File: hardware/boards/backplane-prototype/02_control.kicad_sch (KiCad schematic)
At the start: 14 parts, among them J10 TC2030-IDC-NL SWD, U1 STM32C092GCU6

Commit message: checkpoint before I2C pin move
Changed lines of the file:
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@@
+	(wire
+		(pts
+			(xy 143.51 100.33) (xy 137.16 100.33)
+		)
+		(stroke
+			(width 0)
+			(type default)
+		)
+	)
 	(wire
 		(pts
@@
 		)
 	)
+	(wire
+		(pts
+			(xy 143.51 102.87) (xy 137.16 102.87)
+		)
+		(stroke
+			(width 0)
+			(type default)
+		)
+	)
+	(wire
+		(pts
+			(xy 87.63 105.41) (xy 101.6 105.41)
+		)
+		(stroke
+			(width 0)
+			(type default)
+		)
+	)
 	(label "NRST"
-		(at 101.6 72.39 0)
+		(at 101.6 72.39 180)
 		(effects
 			(font
 				(size 1.27 1.27)
 			)
-			(justify left bottom)
+			(justify right bottom)
 		)
 	)
@@
 	)
 	(label "LED_DATA_RAW"
-		(at 101.6 105.41 180)
+		(at 87.63 105.41 180)
 		(effects
 			(font
@@
 	)
 	(label "SWCLK"
-		(at 137.16 102.87 180)
+		(at 143.51 102.87 0)
 		(effects
 			(font
 				(size 1.27 1.27)
 			)
-			(justify right bottom)
+			(justify left bottom)
 		)
 	)
@@
 	)
 	(label "SWDIO"
-		(at 137.16 100.33 180)
+		(at 143.51 100.33 0)
 		(effects
 			(font
 				(size 1.27 1.27)
 			)
-			(justify right bottom)
+			(justify left bottom)
 		)
 	)

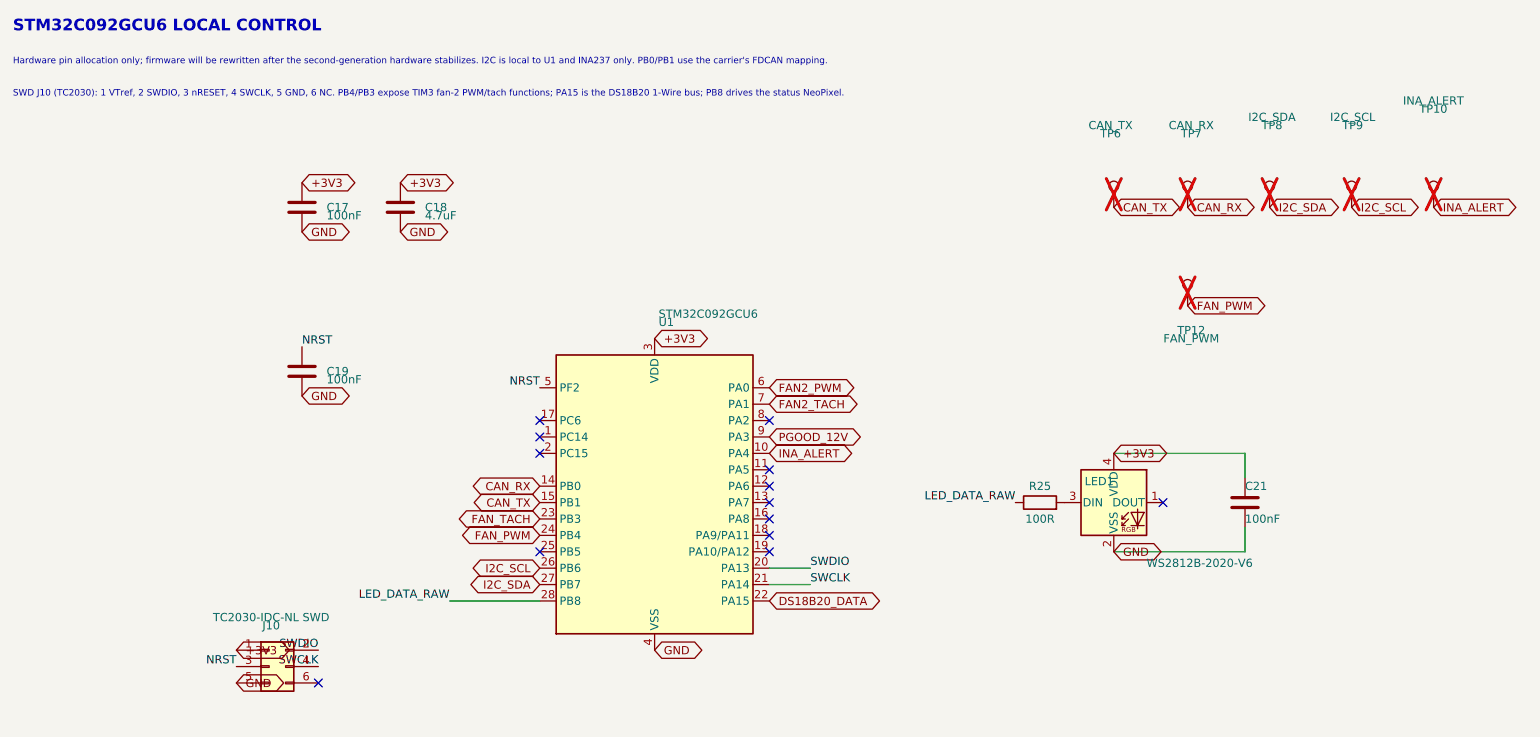
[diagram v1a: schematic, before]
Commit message: move backplane I2C to PA6 and PA7
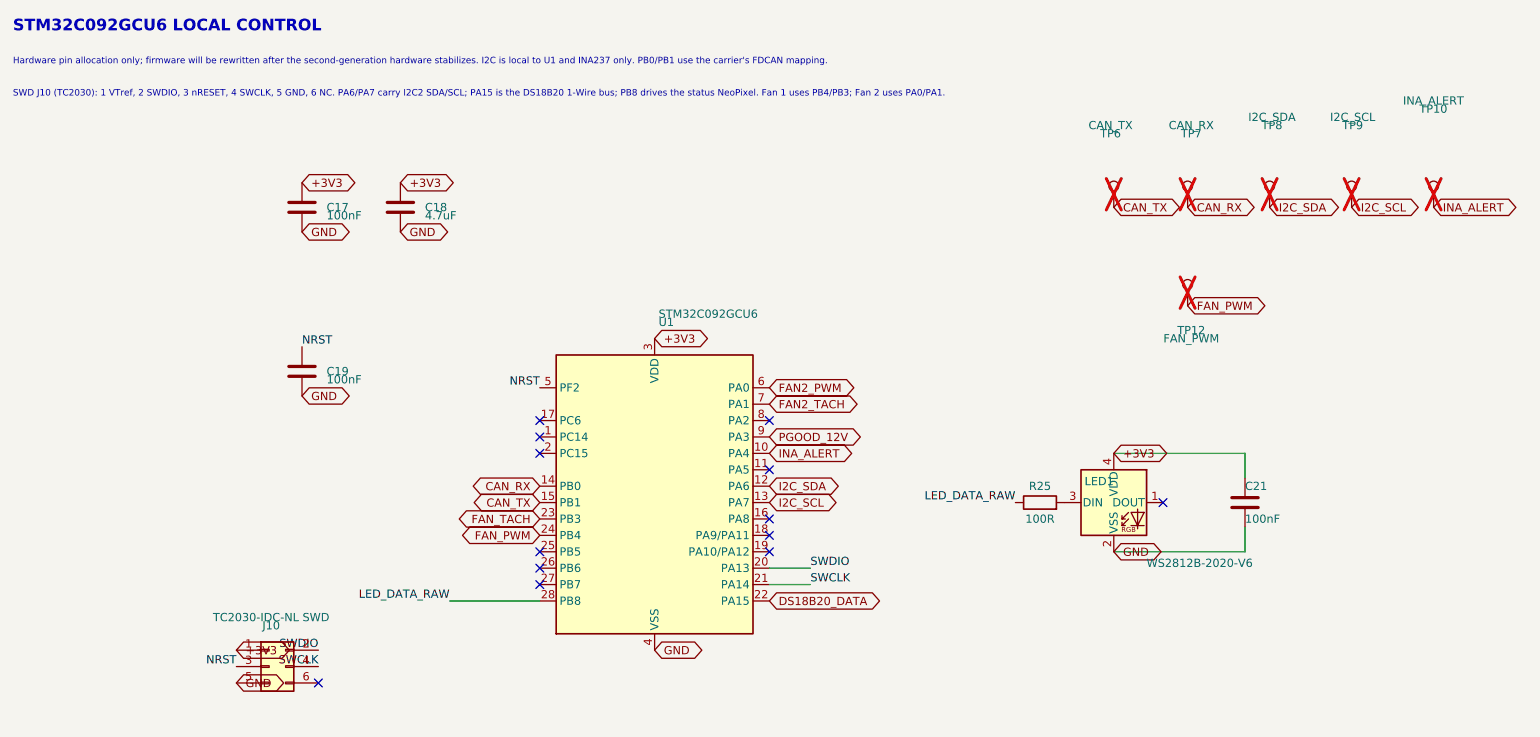
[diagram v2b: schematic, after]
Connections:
- net I2C_SCL: now also U1.13 (PA7); no longer U1.26 (PB6)
- net I2C_SDA: now also U1.12 (PA6); no longer U1.27 (PB7)
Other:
- note added: "SWD J10 (TC2030): 1 VTref, 2 SWDIO, 3 nRESET, 4 SWCLK, 5 GND, 6 NC. PA6/PA7 carry I2C2 SDA/SCL; PA15 is the DS18B20 1-Wire bus; PB8 drives the status NeoPixel. Fan 1 uses PB4/PB3; Fan 2 uses PA0/PA1."
- note removed: "SWD J10 (TC2030): 1 VTref, 2 SWDIO, 3 nRESET, 4 SWCLK, 5 GND, 6 NC. PB4/PB3 expose TIM3 fan-2 PWM/tach functions; PA15 is the DS18B20 1-Wire bus; PB8 drives the status NeoPixel."
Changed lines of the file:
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@@
 	(generator_version "10.0")
 	(paper "A4")
-	(text "SWD J10 (TC2030): 1 VTref, 2 SWDIO, 3 nRESET, 4 SWCLK, 5 GND, 6 NC. PB4/PB3 expose TIM3 fan-2 PWM/tach functions; PA15 is the DS18B20 1-Wire bus; PB8 drives the status NeoPixel."
+	(text "SWD J10 (TC2030): 1 VTref, 2 SWDIO, 3 nRESET, 4 SWCLK, 5 GND, 6 NC. PA6/PA7 carry I2C2 SDA/SCL; PA15 is the DS18B20 1-Wire bus; PB8 drives the status NeoPixel. Fan 1 uses PB4/PB3; Fan 2 uses PA0/PA1."
 		(exclude_from_sim no)
 		(at 20 27.5 0)
@@
 	)
 	(no_connect
-		(at 137.16 87.63)
-	)
-	(no_connect
-		(at 137.16 90.17)
-	)
-	(no_connect
 		(at 137.16 97.79)
 	)
 	(no_connect
 		(at 101.6 82.55)
+	)
+	(no_connect
+		(at 101.6 100.33)
+	)
+	(no_connect
+		(at 101.6 102.87)
 	)
 	(no_connect
@@
 	(global_label "I2C_SCL"
 		(shape bidirectional)
-		(at 101.6 100.33 180)
-		(effects
-			(font
-				(size 1.27 1.27)
-			)
-			(justify right)
-		)
-		(property "Intersheetrefs" "${INTERSHEET_REFS}"
-			(at 101.6 100.33 0)
+		(at 137.16 90.17 0)
+		(effects
+			(font
+				(size 1.27 1.27)
+			)
+			(justify left)
+		)
+		(property "Intersheetrefs" "${INTERSHEET_REFS}"
+			(at 137.16 90.17 0)
 			(hide yes)
 			(show_name no)
@@
 	(global_label "I2C_SDA"
 		(shape bidirectional)
-		(at 101.6 102.87 180)
-		(effects
-			(font
-				(size 1.27 1.27)
-			)
-			(justify right)
-		)
-		(property "Intersheetrefs" "${INTERSHEET_REFS}"
-			(at 101.6 102.87 0)
-			(hide yes)
-			(show_name no)
+		(at 137.16 87.63 0)
+		(effects
+			(font
+				(size 1.27 1.27)
+			)
+			(justify left)
+		)
+		(property "Intersheetrefs" "${INTERSHEET_REFS}"
+			(at 137.16 87.63 0)
+			(hide yes)
+			(show_name no)

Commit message: swap fan2 tach and status LED MCU pins
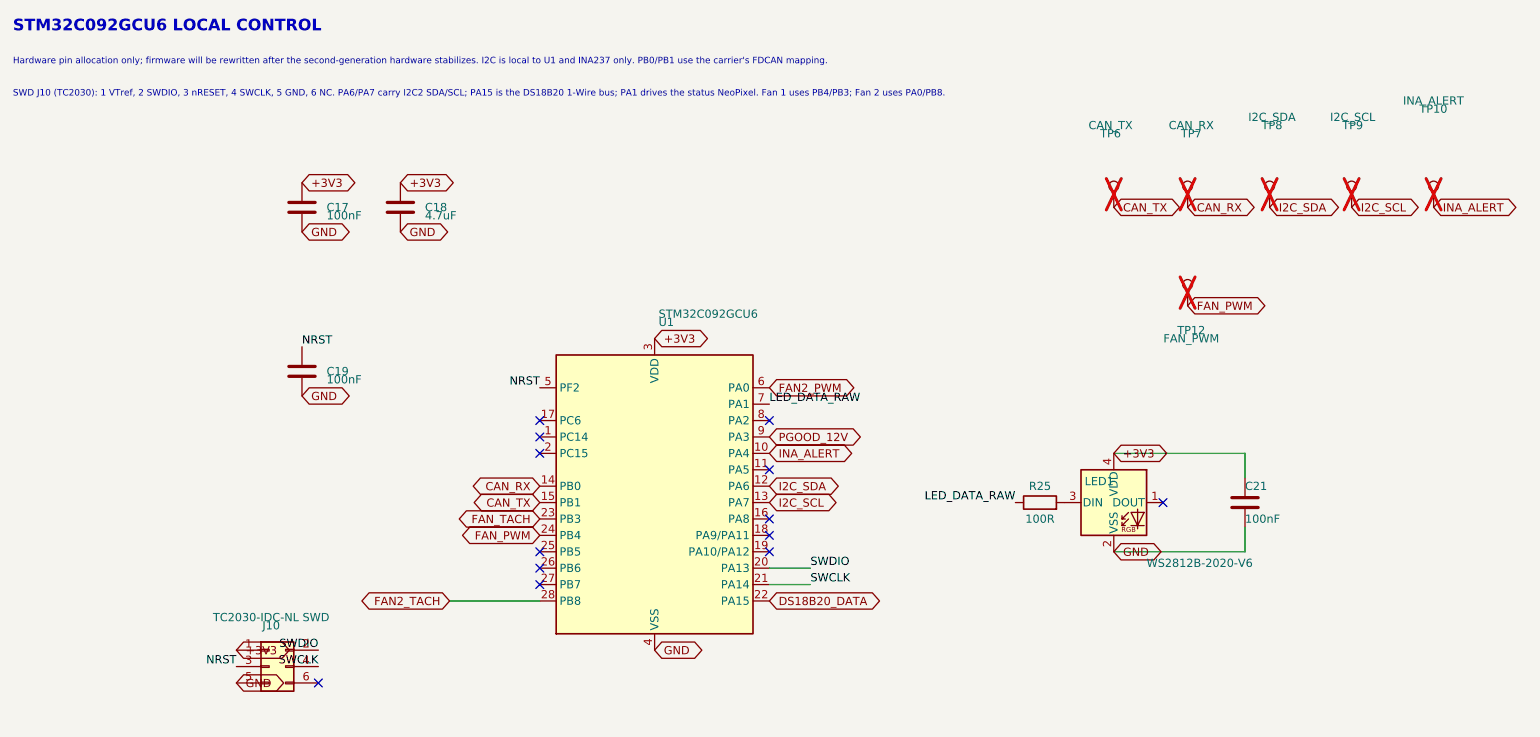
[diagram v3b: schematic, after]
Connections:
- net FAN2_TACH: now also U1.28 (PB8); no longer U1.7 (PA1)
- net LED_DATA_RAW: now also U1.7 (PA1); no longer U1.28 (PB8)
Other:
- note added: "SWD J10 (TC2030): 1 VTref, 2 SWDIO, 3 nRESET, 4 SWCLK, 5 GND, 6 NC. PA6/PA7 carry I2C2 SDA/SCL; PA15 is the DS18B20 1-Wire bus; PA1 drives the status NeoPixel. Fan 1 uses PB4/PB3; Fan 2 uses PA0/PB8."
- note removed: "SWD J10 (TC2030): 1 VTref, 2 SWDIO, 3 nRESET, 4 SWCLK, 5 GND, 6 NC. PA6/PA7 carry I2C2 SDA/SCL; PA15 is the DS18B20 1-Wire bus; PB8 drives the status NeoPixel. Fan 1 uses PB4/PB3; Fan 2 uses PA0/PA1."
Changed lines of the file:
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@@
 	(generator_version "10.0")
 	(paper "A4")
-	(text "SWD J10 (TC2030): 1 VTref, 2 SWDIO, 3 nRESET, 4 SWCLK, 5 GND, 6 NC. PA6/PA7 carry I2C2 SDA/SCL; PA15 is the DS18B20 1-Wire bus; PB8 drives the status NeoPixel. Fan 1 uses PB4/PB3; Fan 2 uses PA0/PA1."
+	(text "SWD J10 (TC2030): 1 VTref, 2 SWDIO, 3 nRESET, 4 SWCLK, 5 GND, 6 NC. PA6/PA7 carry I2C2 SDA/SCL; PA15 is the DS18B20 1-Wire bus; PA1 drives the status NeoPixel. Fan 1 uses PB4/PB3; Fan 2 uses PA0/PB8."
 		(exclude_from_sim no)
 		(at 20 27.5 0)
@@
 	)
 	(label "LED_DATA_RAW"
-		(at 87.63 105.41 180)
-		(effects
-			(font
-				(size 1.27 1.27)
-			)
-			(justify right bottom)
+		(at 137.16 74.93 0)
+		(effects
+			(font
+				(size 1.27 1.27)
+			)
+			(justify left bottom)
 		)
 	)
@@
 	(global_label "FAN2_TACH"
 		(shape bidirectional)
-		(at 137.16 74.93 0)
-		(effects
-			(font
-				(size 1.27 1.27)
-			)
-			(justify left)
-		)
-		(property "Intersheetrefs" "${INTERSHEET_REFS}"
-			(at 137.16 74.93 0)
-			(hide yes)
-			(show_name no)
+		(at 87.63 105.41 180)
+		(effects
+			(font
+				(size 1.27 1.27)
+			)
+			(justify right)
+		)
+		(property "Intersheetrefs" "${INTERSHEET_REFS}"
+			(at 87.63 105.41 180)
+			(hide yes)
+			(show_name no)

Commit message: checkpoint before LED1 3D model fix
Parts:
- removed R25: 100R, Resistor_SMD:R_0603_1608Metric, symbol Device:R
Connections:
- net LED_DATA_RAW: now also LED1.3 (DIN)
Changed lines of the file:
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@@
+	)
+	(no_connect
+		(at 101.6 102.87)
+	)
+	(no_connect
+		(at 101.6 100.33)
 	)
 	(no_connect
@@
 	)
 	(no_connect
-		(at 101.6 100.33)
-	)
-	(no_connect
-		(at 101.6 102.87)
-	)
-	(no_connect
 		(at 137.16 85.09)
 	)
@@
 	(wire
 		(pts
-			(xy 210.82 82.55) (xy 210.82 86.36)
+			(xy 210.82 78.74) (xy 210.82 86.36)
 		)
 		(stroke
@@
 	(wire
 		(pts
-			(xy 190.5 82.55) (xy 210.82 82.55)
+			(xy 190.5 78.74) (xy 210.82 78.74)
 		)
 		(stroke
@@
 	(wire
 		(pts
-			(xy 87.63 105.41) (xy 101.6 105.41)
+			(xy 190.5 78.74) (xy 190.5 82.55)
 		)
 		(stroke
@@
 		)
 	)
+	(wire
+		(pts
+			(xy 87.63 105.41) (xy 101.6 105.41)
+		)
+		(stroke
+			(width 0)
+			(type default)
+		)
+	)
 	(label "NRST"
 		(at 101.6 72.39 180)
@@
 	)
 	(label "LED_DATA_RAW"
-		(at 175.26 90.17 180)
+		(at 182.88 90.17 180)
 		(effects
 			(font
@@
 	(global_label "+3V3"
 		(shape bidirectional)
-		(at 190.5 82.55 0)
-		(effects
-			(font
-				(size 1.27 1.27)
-			)
-			(justify left)
-		)
-		(property "Intersheetrefs" "${INTERSHEET_REFS}"
-			(at 190.5 82.55 0)
+		(at 190.5 78.74 0)
+		(effects
+			(font
+				(size 1.27 1.27)
+			)
+			(justify left)
+		)
+		(property "Intersheetrefs" "${INTERSHEET_REFS}"
+			(at 190.5 78.74 0)
 			(hide yes)
 			(show_name no)
@@
 					(unit 1)
 				)
-			)
-		)
-	)
-	(symbol
-		(lib_id "Device:R")
-		(at 179.07 90.17 90)
-		(unit 1)
-		(body_style 1)
-		(exclude_from_sim no)
-		(in_bom yes)
-		(on_board yes)
-		(in_pos_files yes)
-		(dnp no)
-		(property "Reference" "R25"
-			(at 179.07 87.63 90)
-			(show_name no)
-			(do_not_autoplace no)
-			(effects
-				(font
-					(size 1.27 1.27)
-				)
-			)
-		)
-		(property "Value" "100R"
-			(at 179.07 92.71 90)
-			(show_name no)
-			(do_not_autoplace no)
-			(effects
-				(font
-					(size 1.27 1.27)
-				)
-			)
-		)
-		(property "Footprint" "Resistor_SMD:R_0603_1608Metric"
-			(at 180.848 90.17 90)
-			(hide yes)
-			(show_name no)
-			(do_not_autoplace no)
-			(effects
-				(font
-					(size 1.27 1.27)
-				)
-			)
-		)
-		(property "Datasheet" ""
-			(at 179.07 90.17 0)
-			(hide yes)
-			(show_name no)
-			(do_not_autoplace no)
-			(effects
-				(font
-					(size 1.27 1.27)
-				)
-			)
-		)
-		(property "Description" "Series damping resistor for WS2812B data input"
-			(at 179.07 90.17 0)
-			(hide yes)
-			(show_name no)
-			(do_not_autoplace no)
-			(effects
-				(font
-					(size 1.27 1.27)
-				)
-			)
-		)
-		(property "MPN" "0603WAF1000T5E"
-			(at 179.07 90.17 0)
-			(hide yes)
-			(show_name no)
-			(do_not_autoplace no)
-			(effects
-				(font
-					(size 1.27 1.27)
-				)
-			)
-		)
-		(property "Manufacturer" "UNI-ROYAL (Uniroyal Elec)"
-			(at 179.07 90.17 0)
-			(hide yes)
-			(show_name no)
-			(do_not_autoplace no)
-			(effects
-				(font
-					(size 1.27 1.27)
-				)
-			)
-		)
-		(property "LCSC" "C22775"
-			(at 179.07 90.17 0)
-			(hide yes)
-			(show_name no)
-			(do_not_autoplace no)
-			(effects
-				(font
-					(size 1.27 1.27)
-				)
-			)
-		)
-		(pin "1"
-		)
-		(pin "2"
-		)
-		(instances
-			(project "backplane-prototype"
-				(path "/348cc909-6345-4013-9bef-98714057a65b/4275522b-7aaa-4a22-8d94-d30e15c87e30"
-					(reference "R25")
-					(unit 1)
-				)
